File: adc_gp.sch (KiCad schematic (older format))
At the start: 19 parts, among them U33 INA199C2DCKT, U8 REF5025AIDR

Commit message: updates to gp_dac
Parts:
- IC3: renamed from IC?; footprint QFP65P1600X1600X160-80N -> covg-kicad:QFP65P1600X1600X160-80N
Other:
- moved on the sheet: C22

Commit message: updates to gp ADC
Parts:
- removed C1, C21, C25, C51: 1u, Capacitor_SMD:C_0603_1608Metric, symbol Device:C
- removed C2: 2.2u, Capacitor_SMD:C_0603_1608Metric, symbol Device:C
- removed C26: 0.1u, Capacitor_SMD:C_0603_1608Metric, symbol Device:C
- removed C45: 10u, Capacitor_SMD:C_0603_1608Metric, symbol Device:C
- removed JP5: PINHD-1X04_2.54-SMD, adc_dac_v1:1X04SMD, symbol adc_dac_v1-eagle-import:PINHD-1X04_2.54-SMD
- removed JP7: PINHD-2X06_2.54-SMD, adc_dac_v1:2X06SMD, symbol adc_dac_v1-eagle-import:PINHD-2X06_2.54-SMD
- removed R137: 33, Resistor_SMD:R_0603_1608Metric, symbol Device:R_US
- removed R65: 0, Resistor_SMD:R_0603_1608Metric, symbol Device:R_US
- removed U33: INA199C2DCKT, adc_dac_v1:DCK6_TEX, symbol adc_dac_v1-eagle-import:INA199C2DCKT
- removed U8: REF5025AIDR, adc_dac_v1:D8, symbol adc_dac_v1-eagle-import:REF5025AIDR
- added C100, C93, C95, C96, C97, C99: 0.1u, Capacitor_SMD:C_0603_1608Metric, symbol Device:C
- added C101, C91, C92, C94: 10u, Capacitor_SMD:C_0805_2012Metric, symbol Device:C
- added C71, C72, C73, C74, C75, C76, C77, C78, C79, C80, C81, C82, C83, C84, C85, C86: 1000p, Capacitor_SMD:C_0603_1608Metric, symbol Device:C
- added C87, C88, C89, C90, C98: 10u, Capacitor_SMD:C_0603_1608Metric, symbol Device:C
- added J5: Conn_02x16_Top_Bottom, Connector_PinHeader_2.54mm:PinHeader_2x16_P2.54mm_Horizontal, symbol Connector_Generic:Conn_02x16_Top_Bottom
- added R100, R101, R102, R103, R104, R105, R106, R83, R84, R85, R86, R87, R88, R89, R90, R99: 0, Resistor_SMD:R_0603_1608Metric, symbol Device:R_US
- added R107, R108, R109, R110, R111, R112, R113, R114, R120, R121, R122, R123, R124, R125, R126, R127, R128, R129, R130, R131, R91, R92, R93, R94, R95, R96, R97, R98: 1k, Resistor_SMD:R_0603_1608Metric, symbol Device:R_US
- added R115: 100k, Resistor_SMD:R_0603_1608Metric, symbol Device:R_US
- added R116, R117, R118, R119: 33, Resistor_SMD:R_0603_1608Metric, symbol Device:R_US
- C22: Manf# (none) -> CC0603MRX7R8BB104
- R132: value 50m -> 1k; Manf# (none) -> RC0603FR-071KL
- R134, R135, R136: value 33 -> 1k; Manf# (none) -> RC0603FR-071KL
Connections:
- net labels added: +3.3V, AIN[0], AIN[10], AIN[11], AIN[12], AIN[13], AIN[14], AIN[15], AIN[1], AIN[2], AIN[3], AIN[4], AIN[5], AIN[6], AIN[7], AIN[8], AIN[9], AIN_GND[0], AIN_GND[10], AIN_GND[11], AIN_GND[12], AIN_GND[13], AIN_GND[14], AIN_GND[15], AIN_GND[1], AIN_GND[2], AIN_GND[3], AIN_GND[4], AIN_GND[5], AIN_GND[6], AIN_GND[7], AIN_GND[8], AIN_GND[9], BUSY, CONVST, CSb, IN[0], IN[10], IN[11], IN[12], IN[13], IN[14], IN[15], IN[1], IN[2], IN[3], IN[4], IN[5], IN[6], IN[7], IN[8], IN[9], RESETb, SCLK, SDI, SDOA, SDOB
- net labels removed: +3V3, 2V5_REF, 5V_ISENSE, ADCS_CSB, ADCS_SCLK, ADCS_SDI, ADCS_SDO, DS_OUT0, DS_OUT1, GP_ADC10, GP_ADC3, GP_ADC4, GP_ADC5, GP_ADC6, GP_ADC7, GP_ADC8, GP_ADC9, GP_ISENSE, I_SENSE+, I_SENSE-, TEMP_REF
- wire segments 86 -> 360
- no-connect marks 4 -> 0
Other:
- note added: "AGND_IN must be within \n+/-0.3 V of GND"
- note added: "AVDD bypass (1x 10u, 1x 0.1u per pin)"
- note added: "outputs"
- note removed: "100 V/V gain"
- note removed: "VA+ analog supply. \n5V allows Range 2: VREF*2\nVBD+ is digital I/O supply = 3.3V\nREF from 2V-3V"
- moved on the sheet: C22, IC3

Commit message: completed gp adc
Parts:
- removed J5: Conn_02x16_Top_Bottom, Connector_PinHeader_2.54mm:PinHeader_2x16_P2.54mm_Horizontal, symbol Connector_Generic:Conn_02x16_Top_Bottom
- removed R116: 33, Resistor_SMD:R_0603_1608Metric, symbol Device:R_US
- added J?: Conn_02x16_Odd_Even, symbol Connector_Generic:Conn_02x16_Odd_Even
- C87, C88, C89, C90: Manf# JMK107ABJ106KA-T -> JMK107ABJ106KAHT
- C94: value 10u -> 0.1u; footprint Capacitor_SMD:C_0805_2012Metric -> Capacitor_SMD:C_0603_1608Metric; Manf# GRM21BR70J106KA73L -> CC0603MRX7R8BB104
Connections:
- net labels added: IN[0..15]
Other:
- note added: "AVDD bypass (1x 10uF, 1x 0.1uF per pin)"
- note added: "Board edge"
- note added: "Must by pulled up by FPGA to enable.\n3.3 V level."
- note added: "REFIO: most guidance is 0.1uF bypass (including EVM schematics), \nbut datasheet layout section suggests 10 uF."
- note added: "Some inputs will come from other\nwires and connectors"
- note added: "input"
- note removed: "AVDD bypass (1x 10u, 1x 0.1u per pin)"
- moved on the sheet: R118
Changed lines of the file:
@@
 F 2 "Capacitor_SMD:C_0603_1608Metric" H 5950 900 50  0001 C CNN
 F 3 "" H 5950 900 50  0001 C CNN
-F 4 "JMK107ABJ106KA-T" H 5950 900 50  0001 C CNN "Manf#"
+F 4 "JMK107ABJ106KAHT" H 5950 900 50  0001 C CNN "Manf#"
 	1    5950 900
 	1    0    0    -1
@@
 F 2 "Capacitor_SMD:C_0603_1608Metric" H 6350 900 50  0001 C CNN
 F 3 "" H 6350 900 50  0001 C CNN
-F 4 "JMK107ABJ106KA-T" H 6350 900 50  0001 C CNN "Manf#"
+F 4 "JMK107ABJ106KAHT" H 6350 900 50  0001 C CNN "Manf#"
 	1    6350 900
 	1    0    0    -1
@@
 F 2 "Capacitor_SMD:C_0603_1608Metric" H 6750 900 50  0001 C CNN
 F 3 "" H 6750 900 50  0001 C CNN
-F 4 "JMK107ABJ106KA-T" H 6750 900 50  0001 C CNN "Manf#"
+F 4 "JMK107ABJ106KAHT" H 6750 900 50  0001 C CNN "Manf#"
 	1    6750 900
 	1    0    0    -1
@@
 F 2 "Capacitor_SMD:C_0603_1608Metric" H 7150 900 50  0001 C CNN
 F 3 "" H 7150 900 50  0001 C CNN
-F 4 "JMK107ABJ106KA-T" H 7150 900 50  0001 C CNN "Manf#"
+F 4 "JMK107ABJ106KAHT" H 7150 900 50  0001 C CNN "Manf#"
 	1    7150 900
 	1    0    0    -1
 $EndComp
-Text Notes 11000 850  0    50   ~ 0
-AVDD bypass (1x 10u, 1x 0.1u per pin)
+Text Notes 10300 750  0    50   ~ 0
+AVDD bypass (1x 10uF, 1x 0.1uF per pin)
 $Comp
 L Device:C C?
@@
 AR Path="/6095A004/60EA03DF" Ref="C94"  Part="1"
 F 0 "C94" H 8000 6950 59  0000 L BNN
-F 1 "10u" H 8000 6850 59  0000 L BNN
-F 2 "Capacitor_SMD:C_0805_2012Metric" H 7900 7000 50  0001 C CNN
+F 1 "0.1u" H 8000 6850 59  0000 L BNN
+F 2 "Capacitor_SMD:C_0603_1608Metric" H 7900 7000 50  0001 C CNN
 F 3 "" H 7900 7000 50  0001 C CNN
-F 4 "GRM21BR70J106KA73L" H 7900 7000 50  0001 C CNN "Manf#"
+F 4 "CC0603MRX7R8BB104" H 7900 7000 50  0001 C CNN "Manf#"
 	1    7900 7000
 	1    0    0    -1
@@
 AR Path="/60F1A741" Ref="C?"  Part="1"
 AR Path="/6095A004/60F1A741" Ref="C100"  Part="1"
-F 0 "C100" H 10250 4550 59  0000 L BNN
-F 1 "0.1u" H 10240 4285 59  0000 L BNN
+F 0 "C100" H 9950 4500 59  0000 L BNN
+F 1 "0.1u" H 10000 4300 59  0000 L BNN
 F 2 "Capacitor_SMD:C_0603_1608Metric" H 10200 4450 50  0001 C CNN
 F 3 "" H 10200 4450 50  0001 C CNN
@@
 Wire Wire Line
 	950  8650 1100 8650
-$Comp
-L Connector_Generic:Conn_02x16_Top_Bottom J5
-U 1 1 61019DA2
-P 11900 2950
-F 0 "J5" H 11950 3867 50  0000 C CNN
-F 1 "Conn_02x16_Top_Bottom" H 11950 3776 50  0000 C CNN
-F 2 "Connector_PinHeader_2.54mm:PinHeader_2x16_P2.54mm_Horizontal" H 11900 2950 50  0001 C CNN
-F 3 "~" H 11900 2950 50  0001 C CNN
-F 4 "68021-132HLF" H 11900 2950 50  0001 C CNN "Manf#"
-	1    11900 2950
-	1    0    0    -1
-$EndComp
 $Comp
 L power:+3.3V #PWR0198
@@
 Wire Wire Line
 	6400 5400 5700 5400
-Text Label 5800 3500 0    50   ~ 0
+Text Label 5750 3500 0    50   ~ 0
 AIN_GND[12]
-Text Label 5800 3700 0    50   ~ 0
+Text Label 5750 3700 0    50   ~ 0
 AIN_GND[13]
 Text Label 5800 4200 0    50   ~ 0
@@
 	7900 2600 7900 2050
 Wire Wire Line
-	7900 2050 8550 2050
-Wire Wire Line
 	8900 3800 9400 3800
 $Comp
@@
 Wire Wire Line
 	9500 2200 9700 2200
-$Comp
-L Device:R_US R?
-U 1 1 6197E1A5
-P 9550 3800
-AR Path="/6197E1A5" Ref="R?"  Part="1"
-AR Path="/6095A004/6197E1A5" Ref="R118"  Part="1"
-F 0 "R118" H 9400 3859 59  0000 L BNN
-F 1 "33" H 9400 3670 59  0000 L BNN
-F 2 "Resistor_SMD:R_0603_1608Metric" H 9550 3800 50  0001 C CNN
-F 3 "" H 9550 3800 50  0001 C CNN
-F 4 "RC0603FR-0733RL" H 9550 3800 50  0001 C CNN "Manf#"
-	1    9550 3800
-	0    1    1    0
-$EndComp
 $Comp
 L Device:R_US R?
@@
 Wire Wire Line
 	10100 3900 10300 3900
-Wire Wire Line
-	9700 3800 10300 3800
 $Comp
 L power:GND #GND?
@@
 Text HLabel 9050 2050 2    50   Input ~ 0
 CONVST
-$Comp
-L Device:R_US R?
-U 1 1 61D71BAA
-P 8700 2050
-AR Path="/61D71BAA" Ref="R?"  Part="1"
-AR Path="/6095A004/61D71BAA" Ref="R116"  Part="1"
-F 0 "R116" H 8600 2150 59  0000 L BNN
-F 1 "33" H 8550 1920 59  0000 L BNN
-F 2 "Resistor_SMD:R_0603_1608Metric" H 8700 2050 50  0001 C CNN
-F 3 "" H 8700 2050 50  0001 C CNN
-F 4 "RC0603FR-0733RL" H 8700 2050 50  0001 C CNN "Manf#"
-	1    8700 2050
-	0    -1   -1   0
-$EndComp
-Wire Wire Line
-	8850 2050 9050 2050
-Text HLabel 10300 3800 2    50   Output ~ 0
+Text HLabel 10300 3650 2    50   Output ~ 0
 SDOA
 Text HLabel 10300 3900 2    50   Output ~ 0
@@
 Text HLabel 9400 4000 2    50   Input ~ 0
 SDI
-Text Notes 10600 3850 0    50   ~ 0
+Text Notes 10600 3700 0    50   ~ 0
 outputs
 Text HLabel 8700 7050 2    50   Input ~ 0
@@
 Wire Wire Line
 	11700 3750 11450 3750
-Text Label 11450 2250 0    50   ~ 0
-IN[0]
 Text Label 11450 2350 0    50   ~ 0
 IN[1]
@@
 Wire Wire Line
 	8900 4000 9400 4000
+Text Notes 5950 7650 0    39   ~ 0
+REFIO: most guidance is 0.1uF bypass (including EVM schematics), \nbut datasheet layout section suggests 10 uF.
+Text Notes 8750 7250 0    39   ~ 0
+Must by pulled up by FPGA to enable.\n3.3 V level.
+Wire Wire Line
+	7900 2050 9050 2050
+Text Notes 9150 2000 0    50   ~ 0
+input
+Text Notes 10000 2400 0    50   ~ 0
+input
+Text Notes 10000 2500 0    50   ~ 0
+input
+Wire Wire Line
+	9400 3650 9400 3800
+Wire Wire Line
+	9700 3650 10300 3650
+$Comp
+L Device:R_US R?
+U 1 1 6197E1A5
+P 9550 3650
+AR Path="/6197E1A5" Ref="R?"  Part="1"
+AR Path="/6095A004/6197E1A5" Ref="R118"  Part="1"
+F 0 "R118" H 9400 3709 59  0000 L BNN
+F 1 "33" H 9400 3520 59  0000 L BNN
+F 2 "Resistor_SMD:R_0603_1608Metric" H 9550 3650 50  0001 C CNN
+F 3 "" H 9550 3650 50  0001 C CNN
+F 4 "RC0603FR-0733RL" H 9550 3650 50  0001 C CNN "Manf#"
+	1    9550 3650
+	0    1    1    0
+$EndComp
+Text Notes 11400 4000 0    39   ~ 0
+Some inputs will come from other\nwires and connectors
+Text Label 11450 2250 0    50   ~ 0
+IN[0]
 Wire Bus Line
-	600  700  600  8350
+	3050 9200 600  9200
 Wire Bus Line
 	2600 1100 2600 8750
@@
 	2800 700  2800 8350
 Wire Bus Line
-	3050 700  3050 8350
-Wire Bus Line
 	5050 1100 5050 8750
 Wire Bus Line
 	5250 700  5250 8350
+Wire Bus Line
+	3050 700  3050 9200
+Wire Bus Line
+	600  700  600  9200
+Text HLabel 3050 8950 0    39   Output ~ 0
+IN[0..15]
+$Comp
+L Connector_Generic:Conn_02x16_Odd_Even J?
+U 1 1 628D76E6
+P 11900 2950
+F 0 "J?" H 11950 3867 50  0000 C CNN
+F 1 "Conn_02x16_Odd_Even" H 11950 3776 50  0000 C CNN
+F 2 "" H 11900 2950 50  0001 C CNN
+F 3 "~" H 11900 2950 50  0001 C CNN
+	1    11900 2950
+	1    0    0    -1
+$EndComp
+Text Notes 11450 1950 0    39   ~ 0
+Board edge
 $EndSCHEMATC

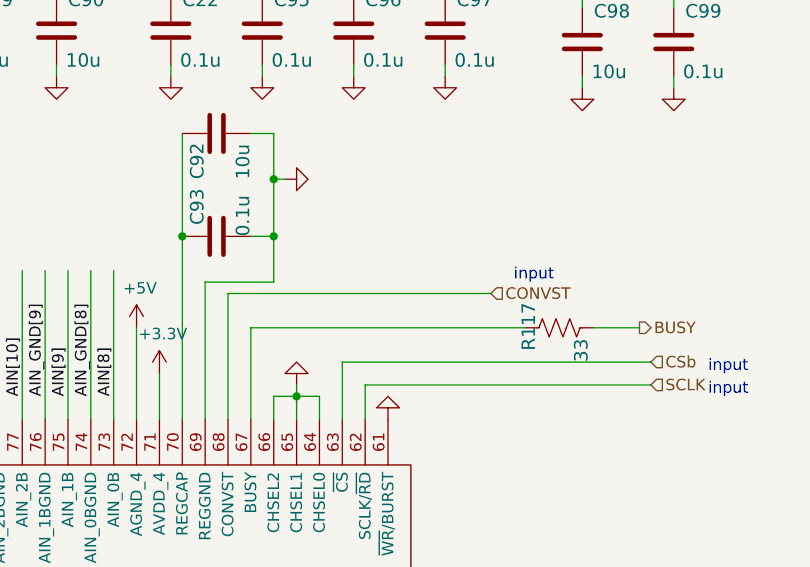
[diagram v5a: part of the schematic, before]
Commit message: moved level shifters to FPGA
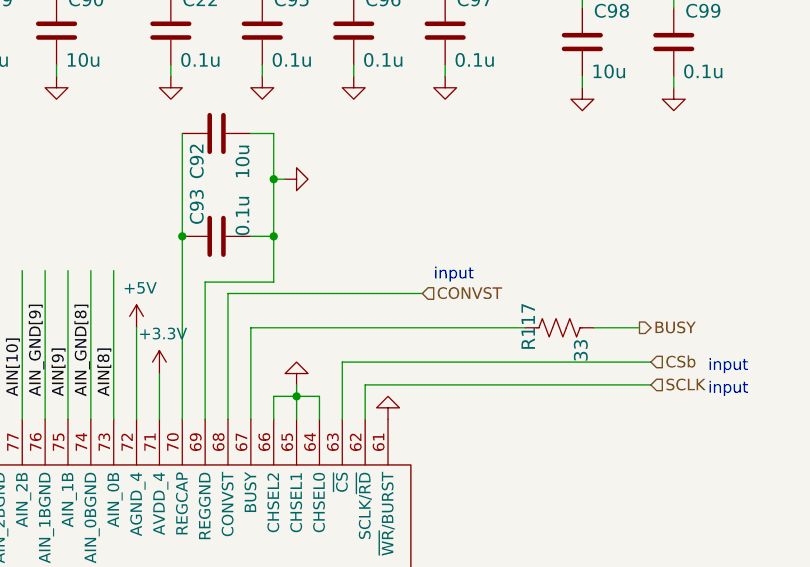
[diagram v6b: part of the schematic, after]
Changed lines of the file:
@@
 Text HLabel 9700 2200 2    50   Output ~ 0
 BUSY
-Text HLabel 9050 2050 2    50   Input ~ 0
+Text HLabel 8750 2050 2    50   Input ~ 0
 CONVST
 Text HLabel 10300 3650 2    50   Output ~ 0
@@
 Must by pulled up by FPGA to enable.\n3.3 V level.
 Wire Wire Line
-	7900 2050 9050 2050
-Text Notes 9150 2000 0    50   ~ 0
+	7900 2050 8750 2050
+Text Notes 8800 2000 0    50   ~ 0
 input
 Text Notes 10000 2400 0    50   ~ 0
@@
 Wire Bus Line
 	3050 9200 600  9200
-Wire Bus Line
-	2600 1100 2600 8750
-Wire Bus Line
-	2800 700  2800 8350
-Wire Bus Line
-	5050 1100 5050 8750
-Wire Bus Line
-	5250 700  5250 8350
-Wire Bus Line
-	3050 700  3050 9200
-Wire Bus Line
-	600  700  600  9200
 Text HLabel 3050 8950 0    39   Output ~ 0
 IN[0..15]
@@
 Text Notes 11450 1950 0    39   ~ 0
 Board edge
+Wire Bus Line
+	2600 1100 2600 8750
+Wire Bus Line
+	2800 700  2800 8350
+Wire Bus Line
+	5050 1100 5050 8750
+Wire Bus Line
+	5250 700  5250 8350
+Wire Bus Line
+	3050 700  3050 9200
+Wire Bus Line
+	600  700  600  9200
 $EndSCHEMATC
